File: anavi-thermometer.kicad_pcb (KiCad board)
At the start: 2 copper layers, 74.9 x 40.6 mm, 25 parts, among them P1 CONN_01X03, U1 I2C_SENS_1, U2 I2C_SENS_1, U3 I2C_SENS_1

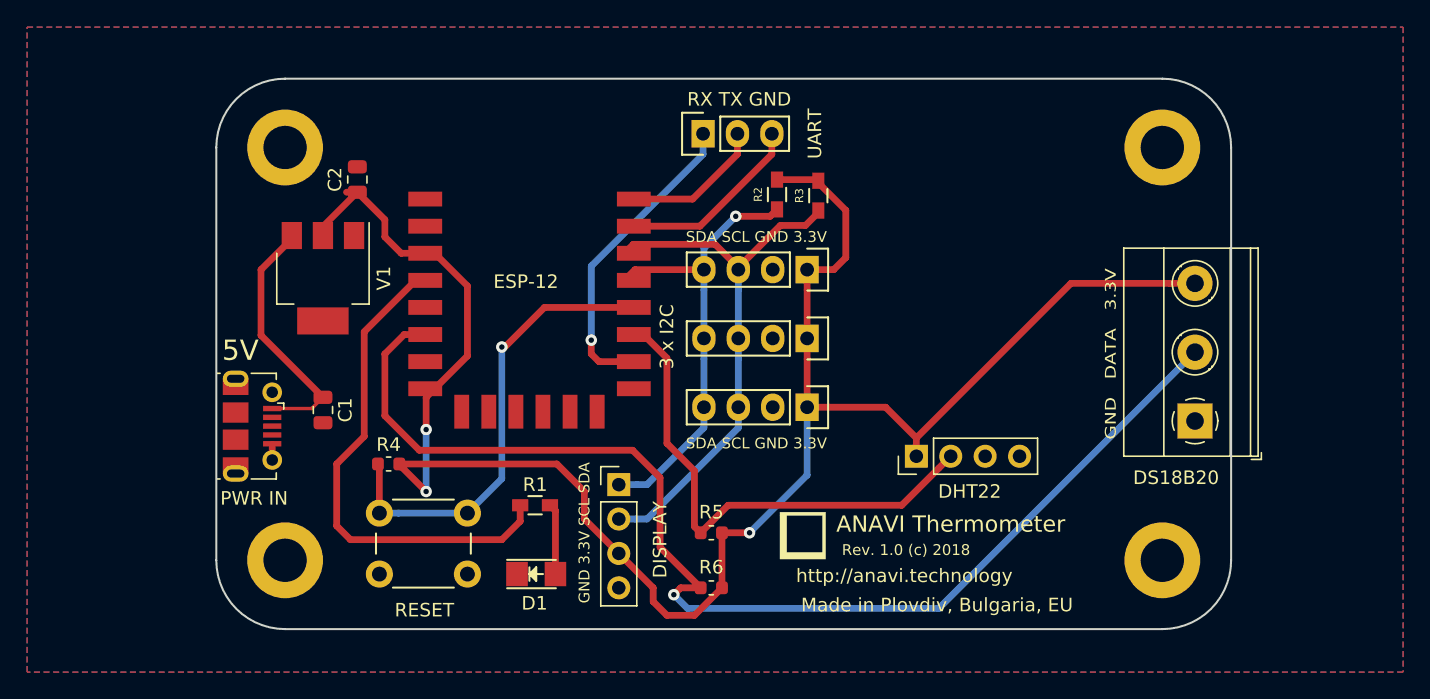
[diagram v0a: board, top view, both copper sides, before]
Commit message: anavi-thermometer.kicad_pcb: Fix UART silkscreen
Fix silkscreen for UART.

Signed-off-by: Leon Anavi <leon@anavi.org>
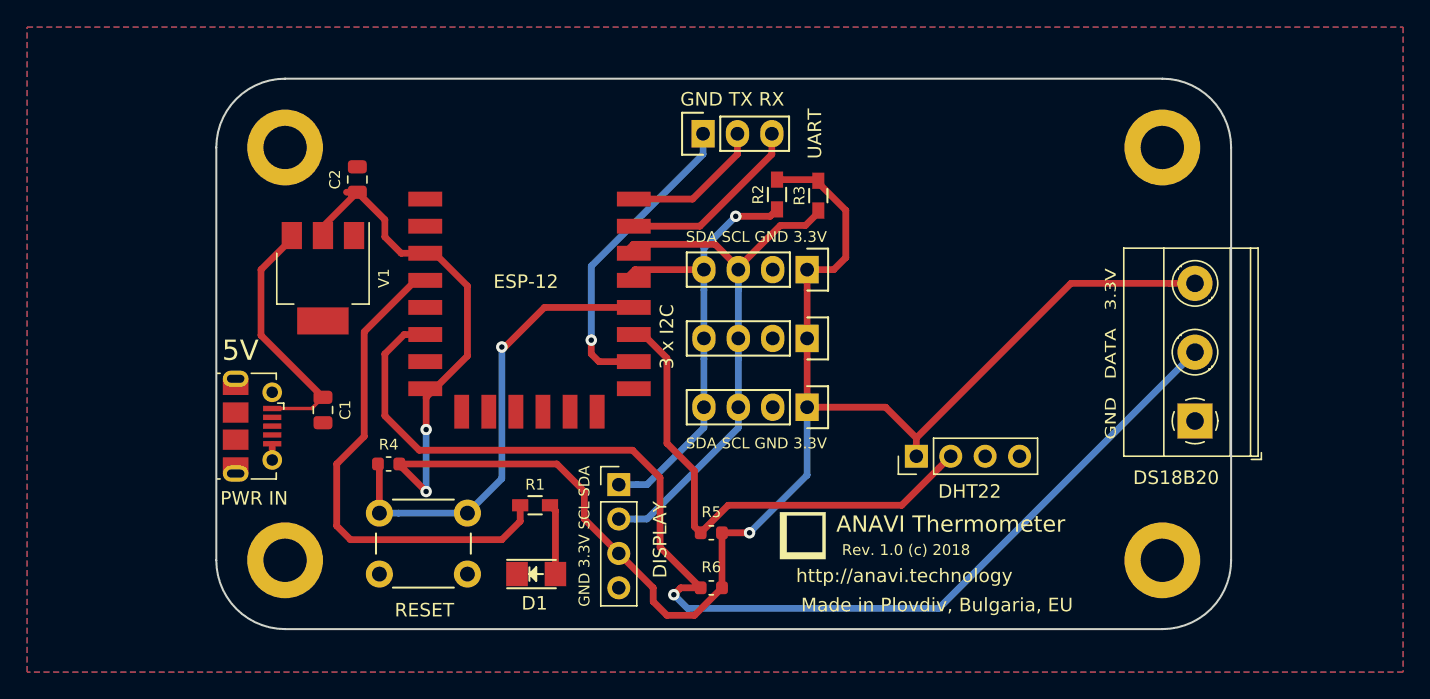
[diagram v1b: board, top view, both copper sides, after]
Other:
- board text added: "GND TX RX"
- board text removed: "RX TX GND"
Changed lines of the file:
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@@
   )
   (setup
-    (last_trace_width 0.254)
+    (last_trace_width 0.5)
     (user_trace_width 0.254)
     (user_trace_width 0.5)
@@
     (attr smd)
     (fp_text reference R1 (at 0 -1.524) (layer F.SilkS)
-      (effects (font (size 1 1) (thickness 0.15)))
-    )
-    (fp_text value 68R (at 0.127 1.524) (layer F.Fab)
+      (effects (font (size 0.8 0.8) (thickness 0.15)))
+    )
+    (fp_text value 68R (at 0.127 0) (layer F.Fab)
       (effects (font (size 1 1) (thickness 0.15)))
     )
@@
     (attr smd)
     (fp_text reference R2 (at 0 1.397 270) (layer F.SilkS)
-      (effects (font (size 0.6 0.6) (thickness 0.1)))
-    )
-    (fp_text value 4,7K (at 0 -1.143 270) (layer F.Fab)
-      (effects (font (size 1 1) (thickness 0.15)))
-    )
+      (effects (font (size 0.8 0.8) (thickness 0.1)))
+    )
+    (fp_text value 4,7K (at 0 0 270) (layer F.Fab)
+      (effects (font (size 1 1) (thickness 0.15)))
+    )
+    (fp_line (start -0.5 -0.675) (end 0.5 -0.675) (layer F.SilkS) (width 0.15))
+    (fp_line (start 0.5 0.675) (end -0.5 0.675) (layer F.SilkS) (width 0.15))
+    (fp_line (start 2 -0.8) (end 2 0.8) (layer F.CrtYd) (width 0.05))
+    (fp_line (start -2 -0.8) (end -2 0.8) (layer F.CrtYd) (width 0.05))
+    (fp_line (start -2 0.8) (end 2 0.8) (layer F.CrtYd) (width 0.05))
+    (fp_line (start -2 -0.8) (end 2 -0.8) (layer F.CrtYd) (width 0.05))
+    (fp_line (start -0.8 -0.4) (end 0.8 -0.4) (layer F.Fab) (width 0.1))
+    (fp_line (start 0.8 -0.4) (end 0.8 0.4) (layer F.Fab) (width 0.1))
+    (fp_line (start 0.8 0.4) (end -0.8 0.4) (layer F.Fab) (width 0.1))
     (fp_line (start -0.8 0.4) (end -0.8 -0.4) (layer F.Fab) (width 0.1))
-    (fp_line (start 0.8 0.4) (end -0.8 0.4) (layer F.Fab) (width 0.1))
-    (fp_line (start 0.8 -0.4) (end 0.8 0.4) (layer F.Fab) (width 0.1))
-    (fp_line (start -0.8 -0.4) (end 0.8 -0.4) (layer F.Fab) (width 0.1))
-    (fp_line (start -2 -0.8) (end 2 -0.8) (layer F.CrtYd) (width 0.05))
-    (fp_line (start -2 0.8) (end 2 0.8) (layer F.CrtYd) (width 0.05))
-    (fp_line (start -2 -0.8) (end -2 0.8) (layer F.CrtYd) (width 0.05))
-    (fp_line (start 2 -0.8) (end 2 0.8) (layer F.CrtYd) (width 0.05))
-    (fp_line (start 0.5 0.675) (end -0.5 0.675) (layer F.SilkS) (width 0.15))
-    (fp_line (start -0.5 -0.675) (end 0.5 -0.675) (layer F.SilkS) (width 0.15))
-    (pad 1 smd rect (at -1.1 0 270) (size 1.2 0.9) (layers F.Cu F.Paste F.Mask)
-      (net 3 +3V3))
     (pad 2 smd rect (at 1.1 0 270) (size 1.2 0.9) (layers F.Cu F.Paste F.Mask)
       (net 4 "Net-(ESP-12-Pad13)"))
+    (pad 1 smd rect (at -1.1 0 270) (size 1.2 0.9) (layers F.Cu F.Paste F.Mask)
+      (net 3 +3V3))
     (model Resistors_SMD.3dshapes/R_0603_HandSoldering.wrl
       (at (xyz 0 0 0))
@@
     (attr smd)
     (fp_text reference R3 (at 0 1.397 270) (layer F.SilkS)
-      (effects (font (size 0.6 0.6) (thickness 0.1)))
-    )
-    (fp_text value 4,7K (at 0.127 -1.27 270) (layer F.Fab)
+      (effects (font (size 0.8 0.8) (thickness 0.1)))
+    )
+    (fp_text value 4,7K (at 0.127 0 270) (layer F.Fab)
       (effects (font (size 1 1) (thickness 0.15)))
     )
@@
     (attr smd)
     (fp_text reference R4 (at 0 -1.43) (layer F.SilkS)
-      (effects (font (size 1 1) (thickness 0.15)))
+      (effects (font (size 0.8 0.8) (thickness 0.15)))
     )
     (fp_text value 2K (at 0 1.43) (layer F.Fab)
@@
     (attr smd)
     (fp_text reference R5 (at 0 1.524 180) (layer F.SilkS)
-      (effects (font (size 1 1) (thickness 0.15)))
+      (effects (font (size 0.8 0.8) (thickness 0.15)))
     )
     (fp_text value 10K (at 0 0 180) (layer F.Fab)
@@
     (attr smd)
     (fp_text reference R6 (at 0 1.524 180) (layer F.SilkS)
-      (effects (font (size 1 1) (thickness 0.15)))
+      (effects (font (size 0.8 0.8) (thickness 0.15)))
     )
     (fp_text value 4,7K (at 0 0 180) (layer F.Fab)
@@
     (attr smd)
     (fp_text reference C1 (at 0 -1.65 270) (layer F.SilkS)
-      (effects (font (size 1 1) (thickness 0.15)))
-    )
-    (fp_text value 10uF (at 0 1.65 270) (layer F.Fab)
+      (effects (font (size 0.8 0.8) (thickness 0.15)))
+    )
+    (fp_text value 10uF (at 0 0 270) (layer F.Fab)
       (effects (font (size 1 1) (thickness 0.15)))
     )
@@
     (attr smd)
     (fp_text reference C2 (at 0 -1.65 90) (layer F.SilkS)
-      (effects (font (size 1 1) (thickness 0.15)))
-    )
-    (fp_text value 10uF (at 0 1.65 90) (layer F.Fab)
+      (effects (font (size 0.8 0.8) (thickness 0.15)))
+    )
+    (fp_text value 10uF (at 0.0785 0 90) (layer F.Fab)
       (effects (font (size 1 1) (thickness 0.15)))
     )
@@
     (attr smd)
     (fp_text reference V1 (at 0 -4.5 270) (layer F.SilkS)
-      (effects (font (size 1 1) (thickness 0.15)))
+      (effects (font (size 0.8 0.8) (thickness 0.15)))
     )
     (fp_text value LD1117S33TR (at 0 4.5 270) (layer F.Fab)
@@
     (effects (font (size 0.8 1) (thickness 0.15)))
   )
-  (gr_text "GND 3.3V SCL SDA" (at 91.948 104.648 90) (layer F.SilkS)
+  (gr_text "GND 3.3V SCL SDA" (at 91.948 104.902 90) (layer F.SilkS)
     (effects (font (size 0.8 0.8) (thickness 0.15)))
   )
-  (gr_text KP-3216EC (at 88.392 109.728) (layer F.Fab)
+  (gr_text KP-3216EC (at 88.9 107.696) (layer F.Fab)
     (effects (font (size 0.8 0.8) (thickness 0.15)))
   )
@@
   (gr_line (start 139.7 106.68) (end 139.7 76.2) (angle 90) (layer Edge.Cuts) (width 0.15))
   (gr_line (start 64.77 106.68) (end 64.77 76.2) (angle 90) (layer Edge.Cuts) (width 0.15))
-  (gr_text "RX TX GND" (at 103.378 72.644) (layer F.SilkS)
+  (gr_text "GND TX RX" (at 102.87 72.644) (layer F.SilkS)
     (effects (font (size 1 1) (thickness 0.15)))
   )
